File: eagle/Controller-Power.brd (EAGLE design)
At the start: 71 x 64 mm, 24 parts, among them IC3 7818TV, X1 MKDSN1,5/2-5,08, X2 MKDSN1,5/2-5,08, X3 MKDSN1,5/2-5,08

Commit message: Lots of schema and board changes
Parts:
- removed C1, C7: 100nF, rcl:C0805
- removed C2, C8: 100µ, rcl:E3,5-8
- removed D1, D3: 1N4004, diode:DO41-10
- removed IC1: (no value), v-reg:317TS
- removed IC3: 7818TV, linear:TO220V
- removed JP2, JP3, JP4: (no value), pinhead:1X02
- removed R1, R20: 100k, rcl:R1206
- removed R2, R21: (no value), pot:PT-10
- removed U$2: GLEICHRICHTER, Gleichrichter:KBPC1
- removed X1, X2, X3: MKDSN1,5/2-5,08, con-phoenix-508:MKDSN1,5/2-5,08
- added TR1: (no value), trafo:EI38-1
- added U$1: GLEICHRICHTER, Gleichrichter:KBPC1
- added X4: MKDSN1,5/2-5,08, con-phoenix-508:MKDSN1,5/2-5,08
- IC2: value (none) -> DCDC-WANDLER; device v-reg:317TS -> 0liver:TRACOPOWER-DCDCWANDER-TSR1
- moved C6 45.6 mm to (55.2, 30.5), turned to 90 degrees
- moved C4 45.5 mm to (52.7, 37.5)
- moved IC2 41.3 mm to (63.5, 33.1)
- moved C5 38.3 mm to (51.4, 30.5), turned to 270 degrees
- moved JP1 3.02 mm to (57.1, 5.71)
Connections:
- removed net N$2: C6.1, IC3.3, JP4.1
- removed net N$24: U$2.AC1, X1.2
- removed net N$28: D3.A, IC1.2, R20.2, X2.2
- removed net N$29: JP1.2, R21.A
- removed net N$3: D1.A, IC2.2, R1.2, X3.2
- removed net N$30: IC1.1, JP1.1, R20.1
- removed net N$4: IC2.1, JP2.1, R1.1
- removed net N$5: JP2.2, R2.A
- new net N$19: TR1.1, X4.1
- new net N$20: TR1.5, X4.2
- new net N$21: TR1.7, U$1.AC2
- new net N$22: TR1.9, U$1.AC1
- net GND: now also IC2.2, JP1.2, U$1.-; no longer C1.2, C2.-, C7.2, C8.-, IC3.2, JP3.1, JP3.2, JP4.2, R2.E, R2.S, R21.E, R21.S, U$2.-, X2.1, X3.1
- net N$17: now also IC2.1, U$1.+; no longer C1.1, C2.+, C7.1, C8.+, D1.C, D3.C, IC1.3, IC2.3, IC3.1, U$2.+
- net N$25: now also C6.1, IC2.3, JP1.1; no longer U$2.AC2, X1.1
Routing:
- net N$17: track 172.6 -> 25.4 mm, vias 2 -> 0
- net GND: track 222.4 -> 94.0 mm
- net N$25: track 42.2 -> 118.2 mm
- net N$2: track 72.1 -> 0.00 mm
- net N$30: track 68.5 -> 0.00 mm
- net N$3: track 65.4 -> 0.00 mm
- net N$4: track 47.2 -> 0.00 mm
- net N$28: track 39.4 -> 0.00 mm
- net N$24: track 28.4 -> 0.00 mm
- net N$21: track 0.00 -> 25.3 mm
- net N$20: track 0.00 -> 18.2 mm
- net N$19: track 0.00 -> 12.9 mm
- net N$29: track 11.6 -> 0.00 mm
- net N$22: track 0.00 -> 11.5 mm
- net N$5: track 4.71 -> 0.00 mm
- added copper zone on layer 16, net N$16
- removed copper zone on layer 16, net N$1
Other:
- board size 71 x 64 mm -> 72 x 49 mm
- board text added: "Spannungsversorgung Controller v1.0"
- board text removed: "36V ~ IN"
- board text removed: "GND"
- board text removed: "Poti V1"
- board text removed: "Poti V2"
- board text removed: "Widerstandskaskade 1"
- board text removed: "Widerstandskaskade 2"

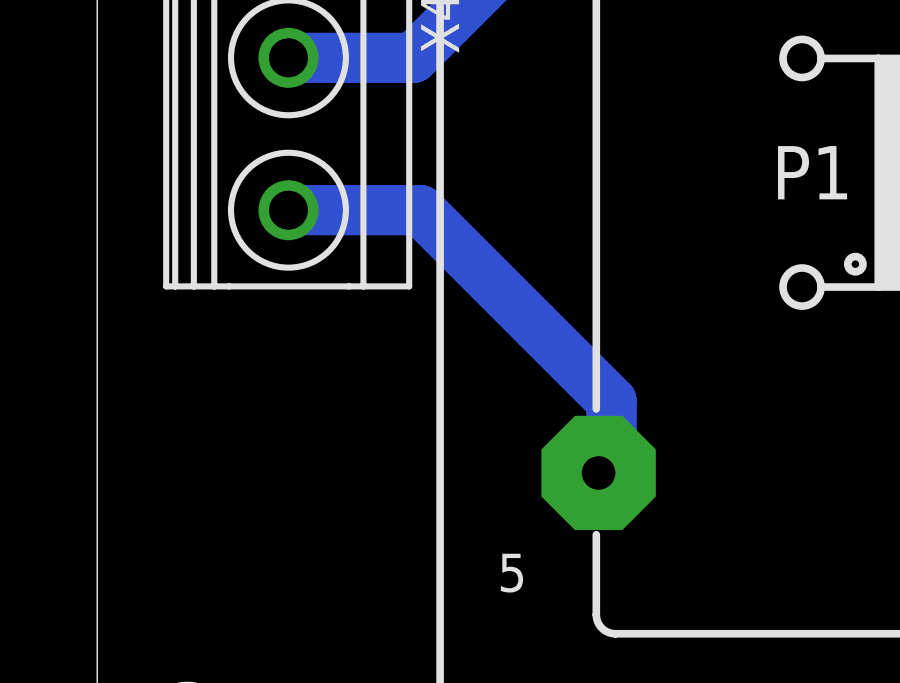
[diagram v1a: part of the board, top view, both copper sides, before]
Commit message: Adjusted drill positions, little size corrections, new pin header
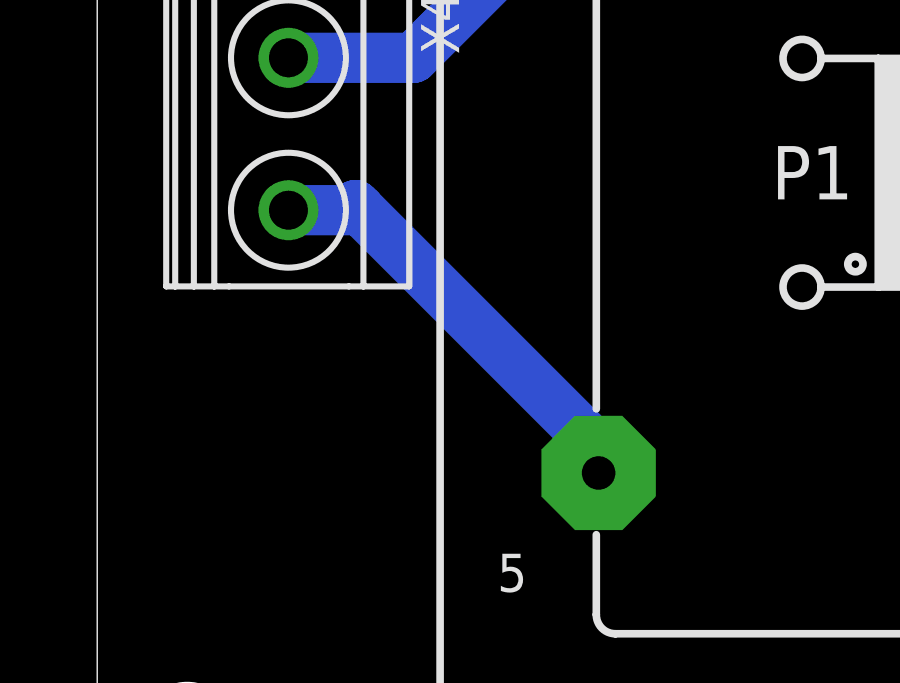
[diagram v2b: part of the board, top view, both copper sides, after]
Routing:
- net N$20: track 18.2 -> 17.5 mm
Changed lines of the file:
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@@
 <setting verticaltext="up"/>
 </settings>
-<grid distance="0.999999999" unitdist="mm" unit="mm" style="lines" multiple="1" display="no" altdistance="25" altunitdist="mil" altunit="mil"/>
+<grid distance="25" unitdist="mil" unit="mil" style="lines" multiple="1" display="no" altdistance="25" altunitdist="mil" altunit="mil"/>
 <layers>
 <layer number="1" name="Top" color="4" fill="1" visible="yes" active="yes"/>
@@
 <hole x="69" y="46" drill="3.2"/>
 <hole x="3" y="46" drill="3.2"/>
-<wire x1="3" y1="28.11" x2="3" y2="29.11" width="0.4064" layer="42"/>
-<wire x1="3" y1="29.11" x2="3" y2="35.11" width="0.4064" layer="42"/>
-<wire x1="3" y1="35.11" x2="21" y2="35.11" width="0.4064" layer="42"/>
-<wire x1="21" y1="35.11" x2="21" y2="8.11" width="0.4064" layer="42"/>
-<wire x1="21" y1="8.11" x2="3" y2="8.11" width="0.4064" layer="42"/>
-<wire x1="3" y1="8.11" x2="3" y2="29.11" width="0.4064" layer="42"/>
+<wire x1="-2" y1="26.11" x2="-2" y2="29.11" width="0.4064" layer="42"/>
+<wire x1="-2" y1="29.11" x2="-2" y2="37.11" width="0.4064" layer="42"/>
+<wire x1="-2" y1="37.11" x2="23" y2="37.11" width="0.4064" layer="42"/>
+<wire x1="23" y1="37.11" x2="23" y2="6.11" width="0.4064" layer="42"/>
+<wire x1="23" y1="6.11" x2="-2" y2="6.11" width="0.4064" layer="42"/>
+<wire x1="-2" y1="6.11" x2="-2" y2="26.11" width="0.4064" layer="42"/>
 <text x="71" y="54" size="1.778" layer="16" rot="MR0">Spannungsversorgung Controller v1.0</text>
-<wire x1="4" y1="34" x2="20" y2="34" width="0.4064" layer="42"/>
-<wire x1="20" y1="34" x2="20" y2="9" width="0.4064" layer="42"/>
-<wire x1="20" y1="9" x2="4" y2="9" width="0.4064" layer="42"/>
-<wire x1="4" y1="9" x2="4" y2="34" width="0.4064" layer="42"/>
+<wire x1="-2" y1="26.11" x2="-2" y2="29.11" width="0.4064" layer="42"/>
+<rectangle x1="10.16" y1="26.035" x2="22.86" y2="36.83" layer="42"/>
+<rectangle x1="10.16" y1="6.35" x2="22.86" y2="16.51" layer="42"/>
+<rectangle x1="0.635" y1="13.97" x2="15.24" y2="30.48" layer="42"/>
+<rectangle x1="14.605" y1="15.875" x2="20.32" y2="26.67" layer="42"/>
+<rectangle x1="7.62" y1="29.21" x2="11.43" y2="33.02" layer="42"/>
+<rectangle x1="7.62" y1="11.43" x2="11.43" y2="15.24" layer="42"/>
 </plain>
 <attributes>
@@
 <contactref element="TR1" pad="5"/>
 <contactref element="X4" pad="2"/>
-<wire x1="6.375" y1="20.3411" x2="10.7739" y2="20.3411" width="1.6764" layer="16"/>
-<wire x1="10.7739" y1="20.3411" x2="14.605" y2="16.51" width="1.6764" layer="16"/>
-<wire x1="14.605" y1="16.51" x2="17.145" y2="13.97" width="1.6764" layer="16"/>
-<wire x1="17.145" y1="13.97" x2="17.145" y2="11.43" width="1.6764" layer="16"/>
+<wire x1="6.375" y1="20.3411" x2="8.7739" y2="20.3411" width="1.6764" layer="16"/>
+<wire x1="8.7739" y1="20.3411" x2="8.605" y2="20.51" width="1.6764" layer="16"/>
+<wire x1="8.605" y1="20.51" x2="17.145" y2="11.97" width="1.6764" layer="16"/>
+<wire x1="17.145" y1="11.97" x2="17.145" y2="11.43" width="1.6764" layer="16"/>
 <wire x1="17.145" y1="11.43" x2="16.51" y2="10.795" width="1.6764" layer="16"/>
 <wire x1="16.51" y1="10.795" x2="17.145" y2="11.43" width="1.6764" layer="16"/>
